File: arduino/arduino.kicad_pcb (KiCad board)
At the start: 2 copper layers, 43.2 x 45.7 mm, 16 parts, among them IC1 ATMEGA328P-P, P1 CONN_6, P2 CONN_2, P3 CONN_6, P4 CONN_6, P5 CONN_1, P6 CONN_6, Q1 16MHz, U1 RFM12B

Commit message: add cladding
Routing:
- added copper zone on B.Cu, net GND
- added copper zone on F.Cu, net GND
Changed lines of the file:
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@@
   (segment (start 103.505 133.985) (end 104.14 133.985) (width 0.254) (layer F.Cu) (net 25))
   (segment (start 104.14 133.985) (end 106.045 132.08) (width 0.254) (layer F.Cu) (net 25))
+  (zone (net 1) (net_name GND) (layer B.Cu) (hatch edge 0.508)
+    (connect_pads (clearance 0.508))
+    (min_thickness 0.254)
+    (fill (arc_segments 16) (thermal_gap 0.508) (thermal_bridge_width 0.508))
+    (polygon
+      (pts
+        (xy 114.935 156.845) (xy 73.025 156.845) (xy 73.025 112.395) (xy 114.935 112.395)
+      )
+    )
+  )
+  (zone (net 1) (net_name GND) (layer F.Cu) (hatch edge 0.508)
+    (connect_pads (clearance 0.508))
+    (min_thickness 0.254)
+    (fill (arc_segments 16) (thermal_gap 0.508) (thermal_bridge_width 0.508))
+    (polygon
+      (pts
+        (xy 114.935 156.845) (xy 73.025 156.845) (xy 73.025 112.395) (xy 114.935 112.395)
+      )
+    )
+  )
 )

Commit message: resize board
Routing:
- removed copper zone on B.Cu, net GND
- removed copper zone on F.Cu, net GND
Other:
- board size 43.2 x 45.7 mm -> 45.7 x 45.7 mm
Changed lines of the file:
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@@
     (area 70.76948 111.6838 115.996721 157.988)
     (thickness 1.6)
-    (drawings 4)
+    (drawings 5)
     (tracks 171)
     (zones 0)
@@
     )
   )
-  (gr_line (start 72.39 157.48) (end 72.39 111.76) (angle 90) (layer Edge.Cuts) (width 0.1))
-  (gr_line (start 115.57 157.48) (end 72.39 157.48) (angle 90) (layer Edge.Cuts) (width 0.1))
-  (gr_line (start 115.57 111.76) (end 115.57 157.48) (angle 90) (layer Edge.Cuts) (width 0.1))
-  (gr_line (start 72.39 111.76) (end 115.57 111.76) (angle 90) (layer Edge.Cuts) (width 0.1))
+  (gr_line (start 71.12 112.395) (end 71.755 112.395) (angle 90) (layer Edge.Cuts) (width 0.1))
+  (gr_line (start 71.12 158.115) (end 71.12 112.395) (angle 90) (layer Edge.Cuts) (width 0.1))
+  (gr_line (start 116.84 158.115) (end 71.12 158.115) (angle 90) (layer Edge.Cuts) (width 0.1))
+  (gr_line (start 116.84 112.395) (end 116.84 158.115) (angle 90) (layer Edge.Cuts) (width 0.1))
+  (gr_line (start 71.755 112.395) (end 116.84 112.395) (angle 90) (layer Edge.Cuts) (width 0.1))
   (segment (start 109.22 129.54) (end 111.76 129.54) (width 0.254) (layer B.Cu) (net 1))
   (segment (start 111.125 133.985) (end 111.125 136.525) (width 0.254) (layer B.Cu) (net 1))
@@
   (segment (start 103.505 133.985) (end 104.14 133.985) (width 0.254) (layer F.Cu) (net 25))
   (segment (start 104.14 133.985) (end 106.045 132.08) (width 0.254) (layer F.Cu) (net 25))
-  (zone (net 1) (net_name GND) (layer B.Cu) (hatch edge 0.508)
-    (connect_pads (clearance 0.508))
-    (min_thickness 0.254)
-    (fill (arc_segments 16) (thermal_gap 0.508) (thermal_bridge_width 0.508))
-    (polygon
-      (pts
-        (xy 114.935 156.845) (xy 73.025 156.845) (xy 73.025 112.395) (xy 114.935 112.395)
-      )
-    )
-  )
-  (zone (net 1) (net_name GND) (layer F.Cu) (hatch edge 0.508)
-    (connect_pads (clearance 0.508))
-    (min_thickness 0.254)
-    (fill (arc_segments 16) (thermal_gap 0.508) (thermal_bridge_width 0.508))
-    (polygon
-      (pts
-        (xy 114.935 156.845) (xy 73.025 156.845) (xy 73.025 112.395) (xy 114.935 112.395)
-      )
-    )
-  )
 )

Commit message: added ground planes
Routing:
- added copper zone on B.Cu, net GND
- added copper zone on F.Cu, net GND
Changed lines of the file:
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@@
     (links 47)
     (no_connects 0)
-    (area 70.76948 111.6838 115.996721 157.988)
+    (area 70.76948 111.6838 116.890001 158.165001)
     (thickness 1.6)
     (drawings 5)
@@
   (segment (start 103.505 133.985) (end 104.14 133.985) (width 0.254) (layer F.Cu) (net 25))
   (segment (start 104.14 133.985) (end 106.045 132.08) (width 0.254) (layer F.Cu) (net 25))
+  (zone (net 1) (net_name GND) (layer B.Cu) (hatch edge 0.508)
+    (connect_pads (clearance 0.508))
+    (min_thickness 0.254)
+    (fill (arc_segments 16) (thermal_gap 0.508) (thermal_bridge_width 0.508))
+    (polygon
+      (pts
+        (xy 116.205 157.48) (xy 71.755 157.48) (xy 71.755 113.03) (xy 116.205 113.03)
+      )
+    )
+  )
+  (zone (net 1) (net_name GND) (layer F.Cu) (hatch edge 0.508)
+    (connect_pads (clearance 0.508))
+    (min_thickness 0.254)
+    (fill (arc_segments 16) (thermal_gap 0.508) (thermal_bridge_width 0.508))
+    (polygon
+      (pts
+        (xy 116.205 157.48) (xy 71.755 157.48) (xy 71.755 113.03) (xy 116.205 113.03)
+      )
+    )
+  )
 )

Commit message: add battery connector
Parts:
- added P7: CONN_2, PIN_ARRAY_2X1, F.Cu at (83.8, 154.3)
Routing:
- net GND: track 89.7 -> 94.4 mm
- net VCC: track 133.6 -> 138.3 mm

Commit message: pcb text
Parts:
- removed P7: CONN_2, PIN_ARRAY_2X1
- added 0V batt +V: battery, PIN_ARRAY_2X1, F.Cu at (83.8, 154.3)
- renumbered U1 to ?, 1PIN to ?, P5 to Ant., P6 to Aux, P3 to P1, P4 to P2, P1 to Rx/Tx, P2 to pwr
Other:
- board text added: "+"
- board text added: "A"
- board text added: "D"
- board text added: "D10"
- board text added: "D6"
- board text added: "D7"
- board text added: "D8"
- board text added: "G"
- board text added: "I"
- board text added: "P"
- board text added: "R"
- board text added: "Radio 1.0"
- board text added: "Rx"
- board text added: "Tx"
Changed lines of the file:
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@@
     (area 70.76948 111.6838 116.890001 158.165001)
     (thickness 1.6)
-    (drawings 5)
+    (drawings 23)
     (tracks 176)
     (zones 0)
@@
     (pad_to_mask_clearance 0)
     (aux_axis_origin 0 0)
-    (visible_elements 7FFFFFFF)
+    (visible_elements 7FFFF7FF)
     (pcbplotparams
       (layerselection 284196865)
@@
   (module SMD-RFM12B (layer F.Cu)
     (at 81.407 123.444 270)
-    (fp_text reference U1 (at 0.1524 9.46912 270) (layer F.SilkS)
+    (fp_text reference "" (at 0.1524 9.46912 270) (layer F.SilkS)
       (effects (font (size 1.524 1.524) (thickness 0.3048)))
     )
@@
     (descr "Connecteur 6 pins")
     (tags "CONN DEV")
-    (fp_text reference P6 (at 0 -2.159 270) (layer F.SilkS)
+    (fp_text reference Aux (at -6.35 3.175 360) (layer F.SilkS)
       (effects (font (size 1.016 1.016) (thickness 0.2032)))
     )
@@
     (descr "Connecteur 6 pins")
     (tags "CONN DEV")
-    (fp_text reference P1 (at 0 -2.159 270) (layer F.SilkS)
+    (fp_text reference Rx/Tx (at -8.255 0 360) (layer F.SilkS)
       (effects (font (size 1.016 1.016) (thickness 0.2032)))
     )
@@
     (descr "Connecteur 6 pins")
     (tags "CONN DEV")
-    (fp_text reference P3 (at 0 -2.159) (layer F.SilkS)
+    (fp_text reference P1 (at -8.89 0) (layer F.SilkS)
       (effects (font (size 1.016 1.016) (thickness 0.2032)))
     )
@@
     (descr "Connecteur 6 pins")
     (tags "CONN DEV")
-    (fp_text reference P4 (at 0 -2.159) (layer F.SilkS)
+    (fp_text reference P2 (at -8.89 0) (layer F.SilkS)
       (effects (font (size 1.016 1.016) (thickness 0.2032)))
     )
@@
     (descr "Connecteurs 2 pins")
     (tags "CONN DEV")
-    (fp_text reference P2 (at 0 -1.905) (layer F.SilkS)
+    (fp_text reference pwr (at 0 -1.905) (layer F.SilkS)
       (effects (font (size 0.762 0.762) (thickness 0.1524)))
     )
@@
     (descr "1 pin")
     (tags "CONN DEV")
-    (fp_text reference P5 (at 0 -1.905) (layer F.SilkS)
+    (fp_text reference Ant. (at 0 2.54) (layer F.SilkS)
       (effects (font (size 0.762 0.762) (thickness 0.1524)))
     )
@@
     (tags DEV)
     (path 1pin)
-    (fp_text reference 1PIN (at 0 -3.048) (layer F.SilkS)
+    (fp_text reference "" (at 0 -3.048) (layer F.SilkS)
       (effects (font (size 1.016 1.016) (thickness 0.254)))
     )
@@
     (tags DEV)
     (path 1pin)
-    (fp_text reference 1PIN (at 0 -3.048) (layer F.SilkS)
+    (fp_text reference "" (at 0 -3.048) (layer F.SilkS)
       (effects (font (size 1.016 1.016) (thickness 0.254)))
     )
@@
     (descr "Connecteurs 2 pins")
     (tags "CONN DEV")
-    (fp_text reference P7 (at 0 -1.905) (layer F.SilkS)
+    (fp_text reference "0V batt +V" (at 0 1.905) (layer F.SilkS)
       (effects (font (size 0.762 0.762) (thickness 0.1524)))
     )
-    (fp_text value CONN_2 (at 0 -1.905) (layer F.SilkS) hide
+    (fp_text value battery (at 0 -1.905) (layer F.SilkS) hide
       (effects (font (size 0.762 0.762) (thickness 0.1524)))
     )
@@
     )
   )
+  (gr_text Tx (at 114.3 146.685) (layer F.SilkS)
+    (effects (font (size 1.5 1.5) (thickness 0.3)))
+  )
+  (gr_text Rx (at 114.3 144.145) (layer F.SilkS)
+    (effects (font (size 1.5 1.5) (thickness 0.3)))
+  )
+  (gr_text + (at 113.665 141.605) (layer F.SilkS)
+    (effects (font (size 1.5 1.5) (thickness 0.3)))
+  )
+  (gr_text G (at 113.665 136.525) (layer F.SilkS)
+    (effects (font (size 1.5 1.5) (thickness 0.3)))
+  )
+  (gr_text R (at 113.665 149.225) (layer F.SilkS)
+    (effects (font (size 1.5 1.5) (thickness 0.3)))
+  )
+  (gr_text "Radio 1.0" (at 96.52 154.305) (layer F.SilkS)
+    (effects (font (size 1.5 1.5) (thickness 0.3)))
+  )
+  (gr_text D10 (at 114.3 114.935) (layer F.SilkS)
+    (effects (font (size 1.5 1.5) (thickness 0.3)))
+  )
+  (gr_text D8 (at 114.3 117.475) (layer F.SilkS)
+    (effects (font (size 1.5 1.5) (thickness 0.3)))
+  )
+  (gr_text D7 (at 114.3 120.015) (layer F.SilkS)
+    (effects (font (size 1.5 1.5) (thickness 0.3)))
+  )
+  (gr_text D6 (at 114.3 122.555) (layer F.SilkS)
+    (effects (font (size 1.5 1.5) (thickness 0.3)))
+  )
+  (gr_text + (at 113.665 125.095) (layer F.SilkS)
+    (effects (font (size 1.5 1.5) (thickness 0.3)))
+  )
+  (gr_text G (at 113.665 127.635) (layer F.SilkS)
+    (effects (font (size 1.5 1.5) (thickness 0.3)))
+  )
+  (gr_text I (at 87.63 137.16) (layer F.SilkS)
+    (effects (font (size 1.5 1.5) (thickness 0.3)))
+  )
+  (gr_text A (at 85.09 137.16) (layer F.SilkS)
+    (effects (font (size 1.5 1.5) (thickness 0.3)))
+  )
+  (gr_text + (at 82.55 137.16) (layer F.SilkS)
+    (effects (font (size 1.5 1.5) (thickness 0.3)))
+  )
+  (gr_text G (at 80.01 137.16) (layer F.SilkS)
+    (effects (font (size 1.5 1.5) (thickness 0.3)))
+  )
+  (gr_text D (at 77.47 137.16) (layer F.SilkS)
+    (effects (font (size 1.5 1.5) (thickness 0.3)))
+  )
+  (gr_text P (at 74.93 137.16) (layer F.SilkS)
+    (effects (font (size 1.5 1.5) (thickness 0.3)))
+  )
   (gr_line (start 71.12 112.395) (end 71.755 112.395) (angle 90) (layer Edge.Cuts) (width 0.1))
   (gr_line (start 71.12 158.115) (end 71.12 112.395) (angle 90) (layer Edge.Cuts) (width 0.1))
@@
   (gr_line (start 116.84 112.395) (end 116.84 158.115) (angle 90) (layer Edge.Cuts) (width 0.1))
   (gr_line (start 71.755 112.395) (end 116.84 112.395) (angle 90) (layer Edge.Cuts) (width 0.1))
-  (segment (start 82.55 154.305) (end 82.55 150.495) (width 0.254) (layer B.Cu) (net 1) (status 400000))
-  (segment (start 82.55 150.495) (end 83.185 149.86) (width 0.254) (layer B.Cu) (net 1) (status 800000))
+  (segment (start 82.55 154.305) (end 82.55 150.495) (width 0.254) (layer B.Cu) (net 1))
+  (segment (start 82.55 150.495) (end 83.185 149.86) (width 0.254) (layer B.Cu) (net 1))
   (segment (start 109.22 129.54) (end 111.76 129.54) (width 0.254) (layer B.Cu) (net 1))
   (segment (start 111.125 133.985) (end 111.125 136.525) (width 0.254) (layer B.Cu) (net 1))
@@
   (segment (start 110.49 144.145) (end 111.125 144.145) (width 0.254) (layer B.Cu) (net 19))
   (segment (start 107.95 146.685) (end 110.49 144.145) (width 0.254) (layer B.Cu) (net 19))
-  (segment (start 93.4847 130.0099) (end 93.4847 130.2004) (width 0.254) (layer B.Cu) (net 20))
-  (segment (start 94.3483 131.064) (end 96.393 131.064) (width 0.254) (layer B.Cu) (net 20))
-  (segment (start 93.4847 130.2004) (end 94.3483 131.064) (width 0.254) (layer B.Cu) (net 20))
+  (segment (start 93.4847 130.0099) (end 93.4847 130.3147) (width 0.254) (layer B.Cu) (net 20))
+  (segment (start 94.615 131.445) (end 95.885 131.445) (width 0.254) (layer B.Cu) (net 20))
+  (segment (start 93.4847 130.3147) (end 94.615 131.445) (width 0.254) (layer B.Cu) (net 20))
   (segment (start 85.09 144.78) (end 85.09 146.685) (width 0.254) (layer B.Cu) (net 21))
   (segment (start 89.535 139.065) (end 95.885 139.065) (width 0.254) (layer B.Cu) (net 21))
@@
   (segment (start 88.265 147.32) (end 88.265 154.94) (width 0.254) (layer F.Cu) (net 24))
   (segment (start 77.47 147.32) (end 88.265 147.32) (width 0.254) (layer F.Cu) (net 24))
-  (segment (start 85.09 154.305) (end 85.09 151.13) (width 0.254) (layer B.Cu) (net 25) (status 400000))
-  (segment (start 85.725 150.495) (end 85.725 149.86) (width 0.254) (layer B.Cu) (net 25) (status C00000))
-  (segment (start 85.09 151.13) (end 85.725 150.495) (width 0.254) (layer B.Cu) (net 25) (status 800000))
+  (segment (start 85.09 154.305) (end 85.09 151.13) (width 0.254) (layer B.Cu) (net 25))
+  (segment (start 85.725 150.495) (end 85.725 149.86) (width 0.254) (layer B.Cu) (net 25))
+  (segment (start 85.09 151.13) (end 85.725 150.495) (width 0.254) (layer B.Cu) (net 25))
   (segment (start 107.315 132.08) (end 107.315 133.985) (width 0.254) (layer F.Cu) (net 25))
   (segment (start 107.315 133.985) (end 106.68 134.62) (width 0.254) (layer F.Cu) (net 25))

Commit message: rotated C
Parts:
- turned C3 to 270 degrees
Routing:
- net VCC: track 138.3 -> 140.0 mm
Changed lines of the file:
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@@
     (thickness 1.6)
     (drawings 23)
-    (tracks 176)
+    (tracks 175)
     (zones 0)
     (modules 17)
@@
   )
   (module C1V5 (layer F.Cu)
-    (at 84.455 149.86 180)
+    (at 84.455 149.86 270)
     (descr "Condensateur e = 1 pas")
     (tags C)
-    (fp_text reference C3 (at 0 -1.26746 180) (layer F.SilkS)
+    (fp_text reference C3 (at 0 -1.26746 270) (layer F.SilkS)
       (effects (font (size 0.762 0.762) (thickness 0.127)))
     )
-    (fp_text value 10u (at 0 1.27 180) (layer F.SilkS)
+    (fp_text value 10u (at 0 1.27 270) (layer F.SilkS)
       (effects (font (size 0.762 0.635) (thickness 0.127)))
     )
-    (fp_text user + (at -2.286 0 180) (layer F.SilkS)
+    (fp_text user + (at -2.286 0 270) (layer F.SilkS)
       (effects (font (size 0.762 0.762) (thickness 0.2032)))
     )
     (fp_circle (center 0 0) (end 0.127 -2.54) (layer F.SilkS) (width 0.127))
-    (pad 1 thru_hole rect (at -1.27 0 180) (size 1.397 1.397) (drill 0.8128)
-      (layers *.Cu *.Mask F.SilkS)
-      (net 25 VCC)
-    )
-    (pad 2 thru_hole circle (at 1.27 0 180) (size 1.397 1.397) (drill 0.8128)
+    (pad 1 thru_hole rect (at -1.27 0 270) (size 1.397 1.397) (drill 0.8128)
+      (layers *.Cu *.Mask F.SilkS)
+      (net 25 VCC)
+    )
+    (pad 2 thru_hole circle (at 1.27 0 270) (size 1.397 1.397) (drill 0.8128)
       (layers *.Cu *.Mask F.SilkS)
       (net 1 GND)
@@
   (gr_line (start 116.84 112.395) (end 116.84 158.115) (angle 90) (layer Edge.Cuts) (width 0.1))
   (gr_line (start 71.755 112.395) (end 116.84 112.395) (angle 90) (layer Edge.Cuts) (width 0.1))
-  (segment (start 82.55 154.305) (end 82.55 150.495) (width 0.254) (layer B.Cu) (net 1))
-  (segment (start 82.55 150.495) (end 83.185 149.86) (width 0.254) (layer B.Cu) (net 1))
+  (segment (start 82.55 151.765) (end 83.82 151.765) (width 0.254) (layer B.Cu) (net 1))
+  (segment (start 83.82 151.765) (end 84.455 151.13) (width 0.254) (layer B.Cu) (net 1) (status 800000))
+  (segment (start 80.01 149.225) (end 82.55 151.765) (width 0.254) (layer B.Cu) (net 1) (status 400000))
+  (segment (start 82.55 151.765) (end 82.55 154.305) (width 0.254) (layer B.Cu) (net 1) (status 800000))
   (segment (start 109.22 129.54) (end 111.76 129.54) (width 0.254) (layer B.Cu) (net 1))
   (segment (start 111.125 133.985) (end 111.125 136.525) (width 0.254) (layer B.Cu) (net 1))
@@
   (segment (start 83.37296 124.46) (end 83.37296 115.52936) (width 0.254) (layer F.Cu) (net 1))
   (segment (start 87.40648 128.49352) (end 83.37296 124.46) (width 0.254) (layer F.Cu) (net 1))
-  (segment (start 80.01 149.225) (end 81.915 149.225) (width 0.254) (layer B.Cu) (net 1))
-  (segment (start 82.55 149.86) (end 83.185 149.86) (width 0.254) (layer B.Cu) (net 1))
-  (segment (start 81.915 149.225) (end 82.55 149.86) (width 0.254) (layer B.Cu) (net 1))
   (segment (start 80.01 144.78) (end 80.01 149.225) (width 0.254) (layer B.Cu) (net 1))
   (segment (start 80.01 139.7) (end 80.01 144.78) (width 0.254) (layer B.Cu) (net 1))
@@
   (segment (start 88.265 147.32) (end 88.265 154.94) (width 0.254) (layer F.Cu) (net 24))
   (segment (start 77.47 147.32) (end 88.265 147.32) (width 0.254) (layer F.Cu) (net 24))
-  (segment (start 85.09 154.305) (end 85.09 151.13) (width 0.254) (layer B.Cu) (net 25))
-  (segment (start 85.725 150.495) (end 85.725 149.86) (width 0.254) (layer B.Cu) (net 25))
-  (segment (start 85.09 151.13) (end 85.725 150.495) (width 0.254) (layer B.Cu) (net 25))
+  (segment (start 84.455 148.59) (end 86.36 148.59) (width 0.254) (layer B.Cu) (net 25) (status 400000))
+  (segment (start 85.09 153.67) (end 85.09 154.305) (width 0.254) (layer B.Cu) (net 25) (status C00000))
+  (segment (start 86.36 152.4) (end 85.09 153.67) (width 0.254) (layer B.Cu) (net 25) (status 800000))
+  (segment (start 86.36 148.59) (end 86.36 152.4) (width 0.254) (layer B.Cu) (net 25))
+  (segment (start 82.55 144.78) (end 82.55 147.32) (width 0.254) (layer B.Cu) (net 25) (status 400000))
+  (segment (start 83.82 148.59) (end 84.455 148.59) (width 0.254) (layer B.Cu) (net 25) (status C00000))
+  (segment (start 82.55 147.32) (end 83.82 148.59) (width 0.254) (layer B.Cu) (net 25) (status 800000))
   (segment (start 107.315 132.08) (end 107.315 133.985) (width 0.254) (layer F.Cu) (net 25))
   (segment (start 107.315 133.985) (end 106.68 134.62) (width 0.254) (layer F.Cu) (net 25))
@@
   (segment (start 90.17 128.905) (end 95.885 128.905) (width 0.254) (layer F.Cu) (net 25))
   (segment (start 85.40496 124.13996) (end 90.17 128.905) (width 0.254) (layer F.Cu) (net 25))
-  (segment (start 82.55 144.78) (end 82.55 147.32) (width 0.254) (layer B.Cu) (net 25))
-  (segment (start 83.82 147.955) (end 85.725 149.86) (width 0.254) (layer B.Cu) (net 25))
-  (segment (start 83.185 147.955) (end 83.82 147.955) (width 0.254) (layer B.Cu) (net 25))
-  (segment (start 82.55 147.32) (end 83.185 147.955) (width 0.254) (layer B.Cu) (net 25))
   (segment (start 74.93 144.78) (end 74.93 149.225) (width 0.254) (layer B.Cu) (net 25))
   (segment (start 74.93 144.78) (end 74.93 142.875) (width 0.254) (layer F.Cu) (net 25))

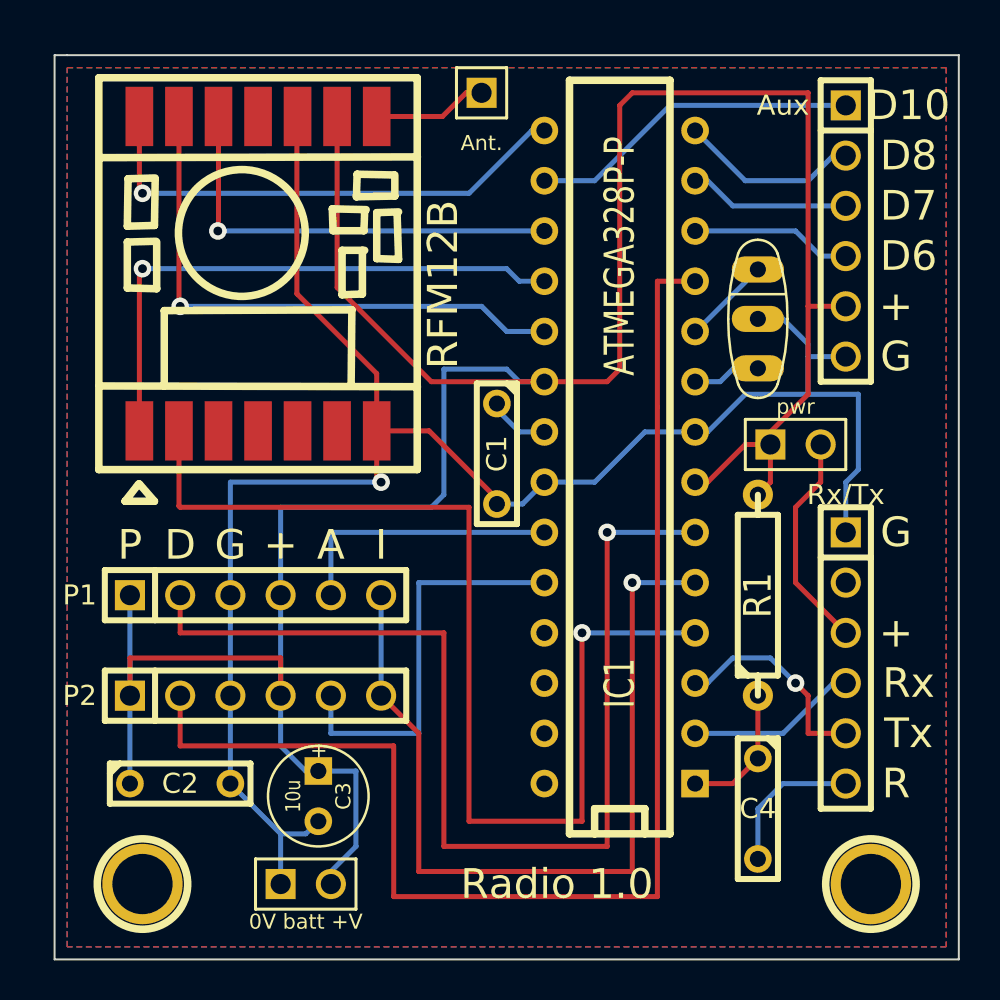
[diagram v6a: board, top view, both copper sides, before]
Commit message: thicken power traces
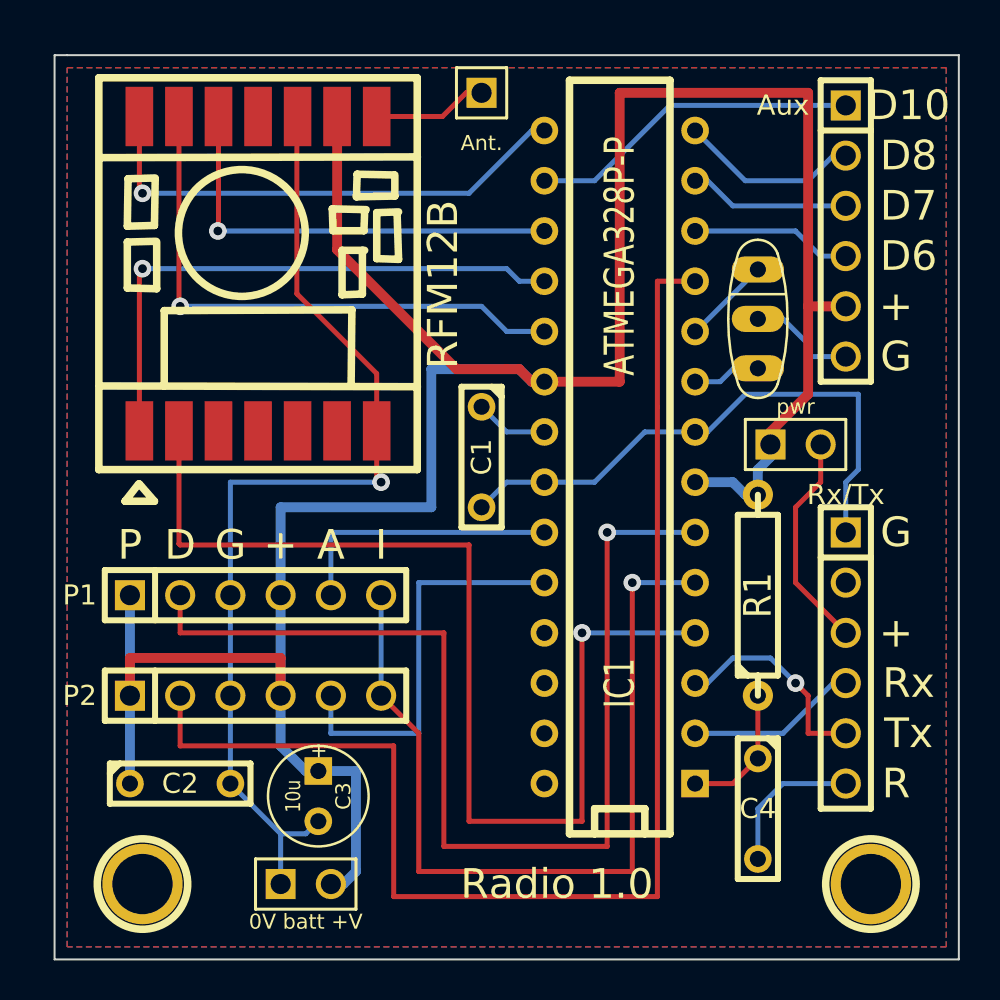
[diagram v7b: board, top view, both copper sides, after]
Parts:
- moved C1 0.79 mm to (92.7, 132.7)
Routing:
- net GND: track 94.5 -> 85.7 mm
- net VCC: track 140.0 -> 139.2 mm
- net N-0000035: track 3.17 -> 3.70 mm
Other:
- net class power added: clearance 0.254, trace_width 0.5, via_dia 0.889, via_drill 0.635
